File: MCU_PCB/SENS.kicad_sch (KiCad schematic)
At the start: 10 parts

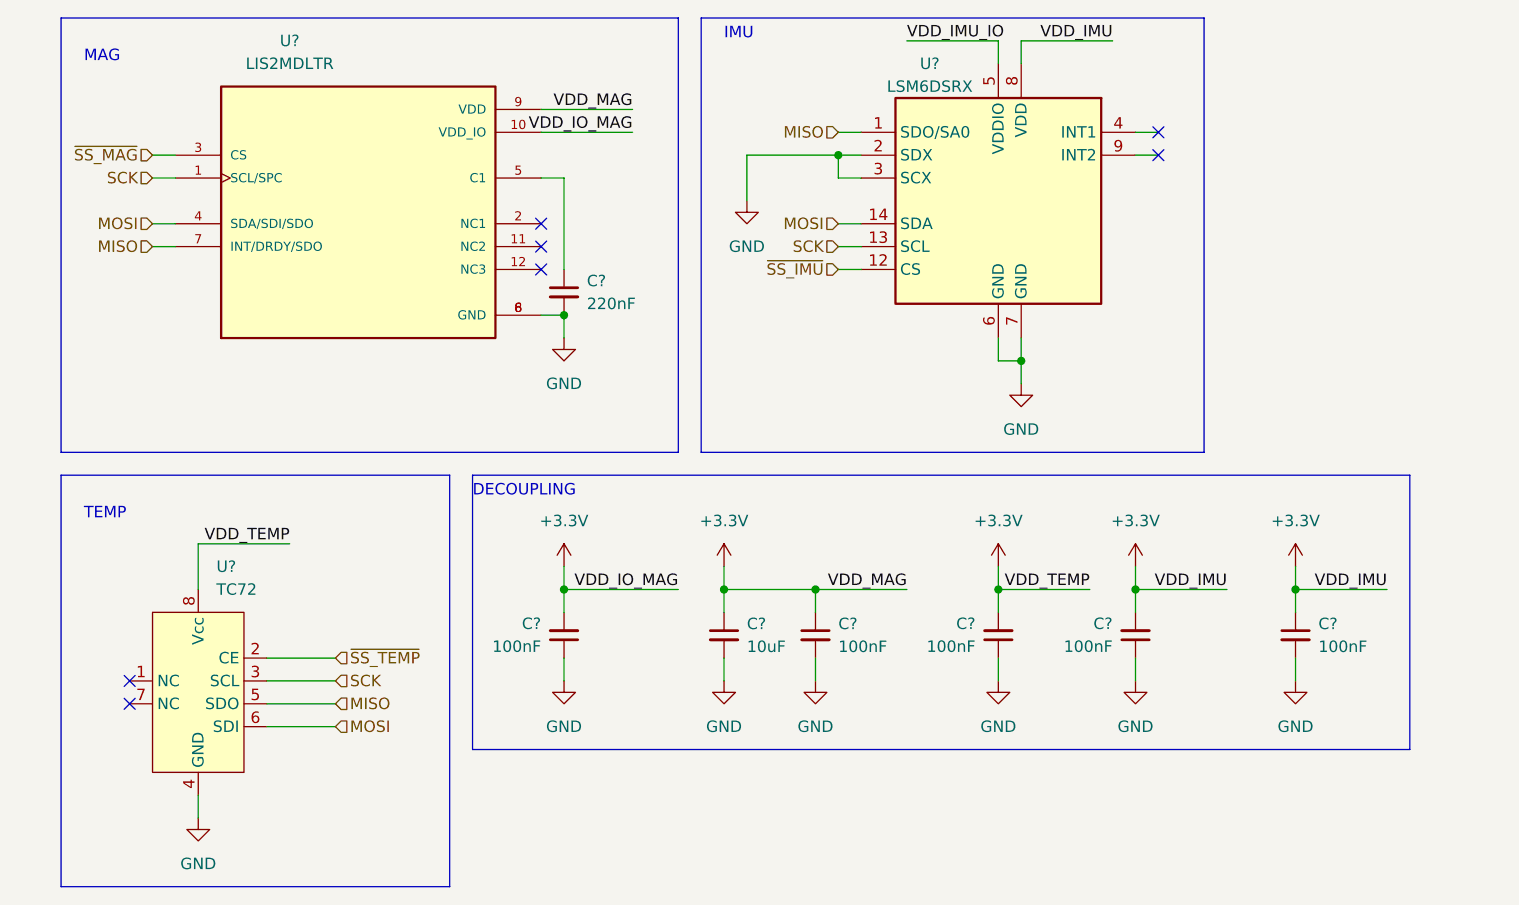
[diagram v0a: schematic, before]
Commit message: 0.1v MCU KiCad
Aesthetics needs to be improved.
Trace width needs to be changed.
More sufficient grounding.
Component placement could be changed.
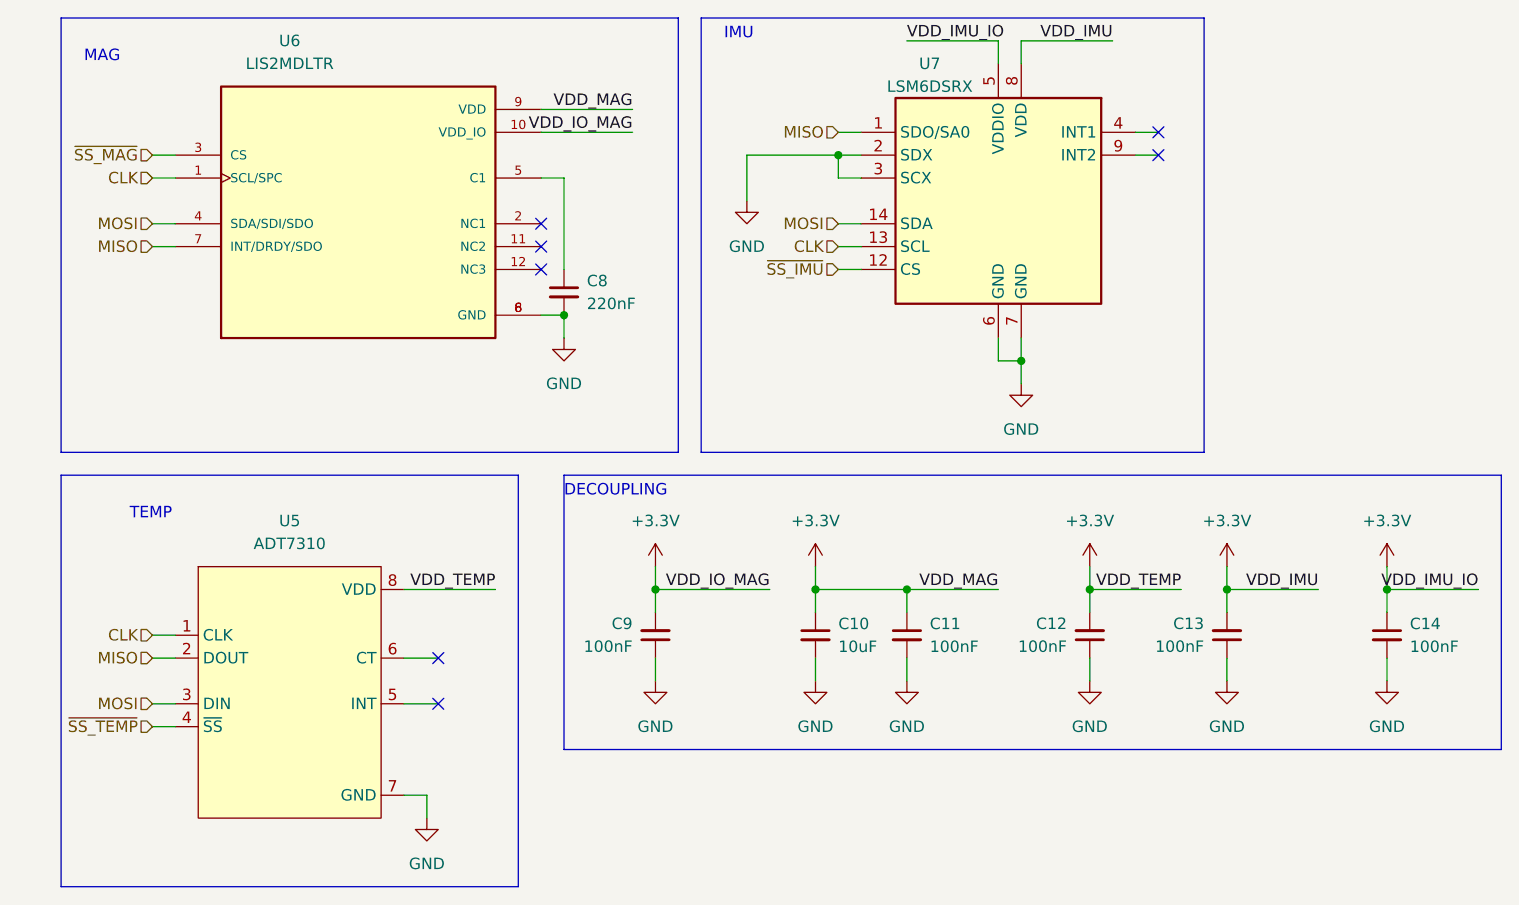
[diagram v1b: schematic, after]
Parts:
- removed U?: TC72, symbol schematics:TC72
- added U5: ADT7310, Package_SO:SOIC-8_3.9x4.9mm_P1.27mm, symbol schematics:ADT7310
- C10, C11, C12, C13, C14, C8, C9: renamed from C?; footprint (none) -> Capacitor_SMD:C_0402_1005Metric
- gave numbers to parts that had none: 2
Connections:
- net VDD_IMU_IO is gone; now on net +3V3: U7.5 (VDDIO)
- net +3V3: now also U5.8 (VDD)
- net GND: now also U5.7 (GND)
- net MISO: now also U5.2 (DOUT)
- net MOSI: now also U5.3 (DIN)
- net ~{SS_TEMP}: now also U5.4 (~{SS})
- net SCK renamed CLK
- net CLK: now also U5.1 (CLK)
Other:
- moved on the sheet: C10, C11, C12, C13, C14, C9
